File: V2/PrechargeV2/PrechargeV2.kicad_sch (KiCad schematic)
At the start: 51 parts, among them J1 430450428, J2 430450428, J4 436500228, U1 TEA 1-0505E, U2 AMC1351DWVR, U3 AMC1351DWVR, U6 OP284EPZ

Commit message: V2
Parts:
- removed CR1, CR2: B240A-13-F, PreChargeParts:SMA_DIO-L, symbol RelayFlyback:B240A-13-F
- removed MOSFET1, MOSFET2: DMN3404L-7, PreChargeParts:SOT23_DIO-L, symbol RelayFET:DMN3404L-7
- removed U1: TEA 1-0505E, PreChargeParts:TEA 1E_TRP, symbol Isolating DC-DC Converter:TEA_1-0505E
- removed U6: OP284EPZ, OP284:N_8_ADI, symbol OP284:OP284EPZ
- added CR1, CR2: B240A-13-F, RelayDriver:SMA_DIO, symbol RelayDriver:B240A-13-F
- added MOSFET1, MOSFET2: DMN3404L-7, RelayDriver:SOT23_DIO, symbol RelayDriver:DMN3404L-7
- added U1: NMV1S0505SC, 5V-5V:SIP4_NMV1S0_MUR, symbol 5V-5V:NMV1S0505SC
- added U4: TLV9002QDGKRQ1, TLV9002:VSSOP8_DGK_TEX, symbol TLV9002:TLV9002QDGKRQ1
- R1, R10, R11, R12, R13, R14, R15, R16, R17, R18, R2, R21, R22, R23, R24, R25, R26, R27, R28, R3, R4, R5, R6, R7, R8, R9: footprint Resistor_THT:R_Axial_DIN0207_L6.3mm_D2.5mm_P10.16mm_Horizontal -> Resistor_SMD:R_0603_1608Metric_Pad0.98x0.95mm_HandSolder
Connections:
- net +5: now also U1.1 (+VIN), U4.8 (V+)
- net GND: now also MOSFET1.2 (S), MOSFET2.2 (S), U1.2 (-VIN), U4.4 (V-); no longer J1.4
- net HV+5: now also U1.7 (+VOUT)
- net HVGND: now also U1.5 (-VOUT); no longer R6.1, U2.3 (GND1), U2.4 (GND1)
- net ShutdownIn: now also J1.3, CR1.1, CR2.1; no longer J1.1
- net at C10.1, R21.2, R23.2: now also U4.5 (IN2+)
- net at C9.1, R22.2, R24.2: now also U4.6 (IN2-)
- net at C6.1, R10.2, R12.2: now also U4.3 (IN1+)
- net at C7.1, R11.2, R9.2: now also U4.2 (IN1-)
- net at R25.2, R26.1: now also MOSFET1.1 (G)
- net at J1.2: now also CR1.2, MOSFET1.3 (D)
- net at A1.A2, C9.2, R24.1: now also U4.7 (OUT2)
- net at A1.A7, C7.2, R11.1: now also U4.1 (OUT1)
- net at R27.1: now also A1.D9; no longer A1.D3
- net at R27.2, R28.1: now also MOSFET2.1 (G)
- net nCS: now reaches A1.D10
- net SI: now reaches A1.D11 (D11_MOSI)
- net SO: now reaches A1.D12 (D12_MISO)
- net SCK: now reaches A1.D13 (D13_SCK)
- net CANInt: now reaches A1.D8
- net InverterGND renamed INVGND
- net INVGND: now also R6.1, U2.3 (GND1), U2.4 (GND1)
- new net: CR2.2, J1.1, MOSFET2.3 (D)
- new net PrechargeStatus: A1.D3, J1.4
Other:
- added sheet CANBUS (CANBUS.kicad_sch)
- moved on the sheet: C11, C12, R7, R8

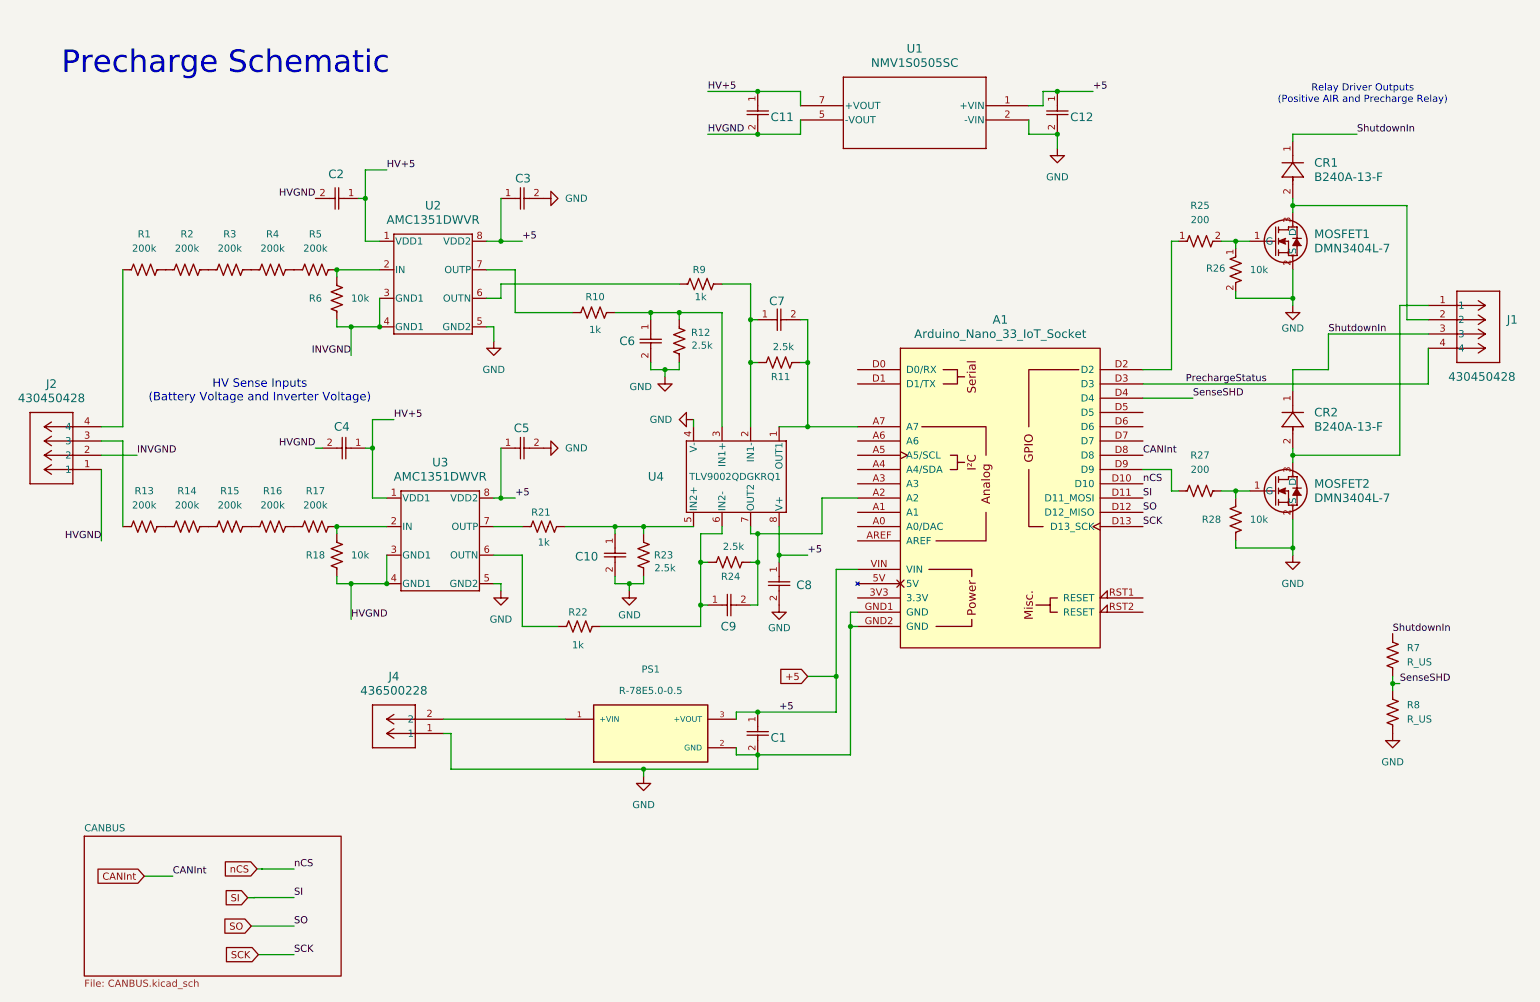
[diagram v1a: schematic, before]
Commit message: Updated Schematic For ESF
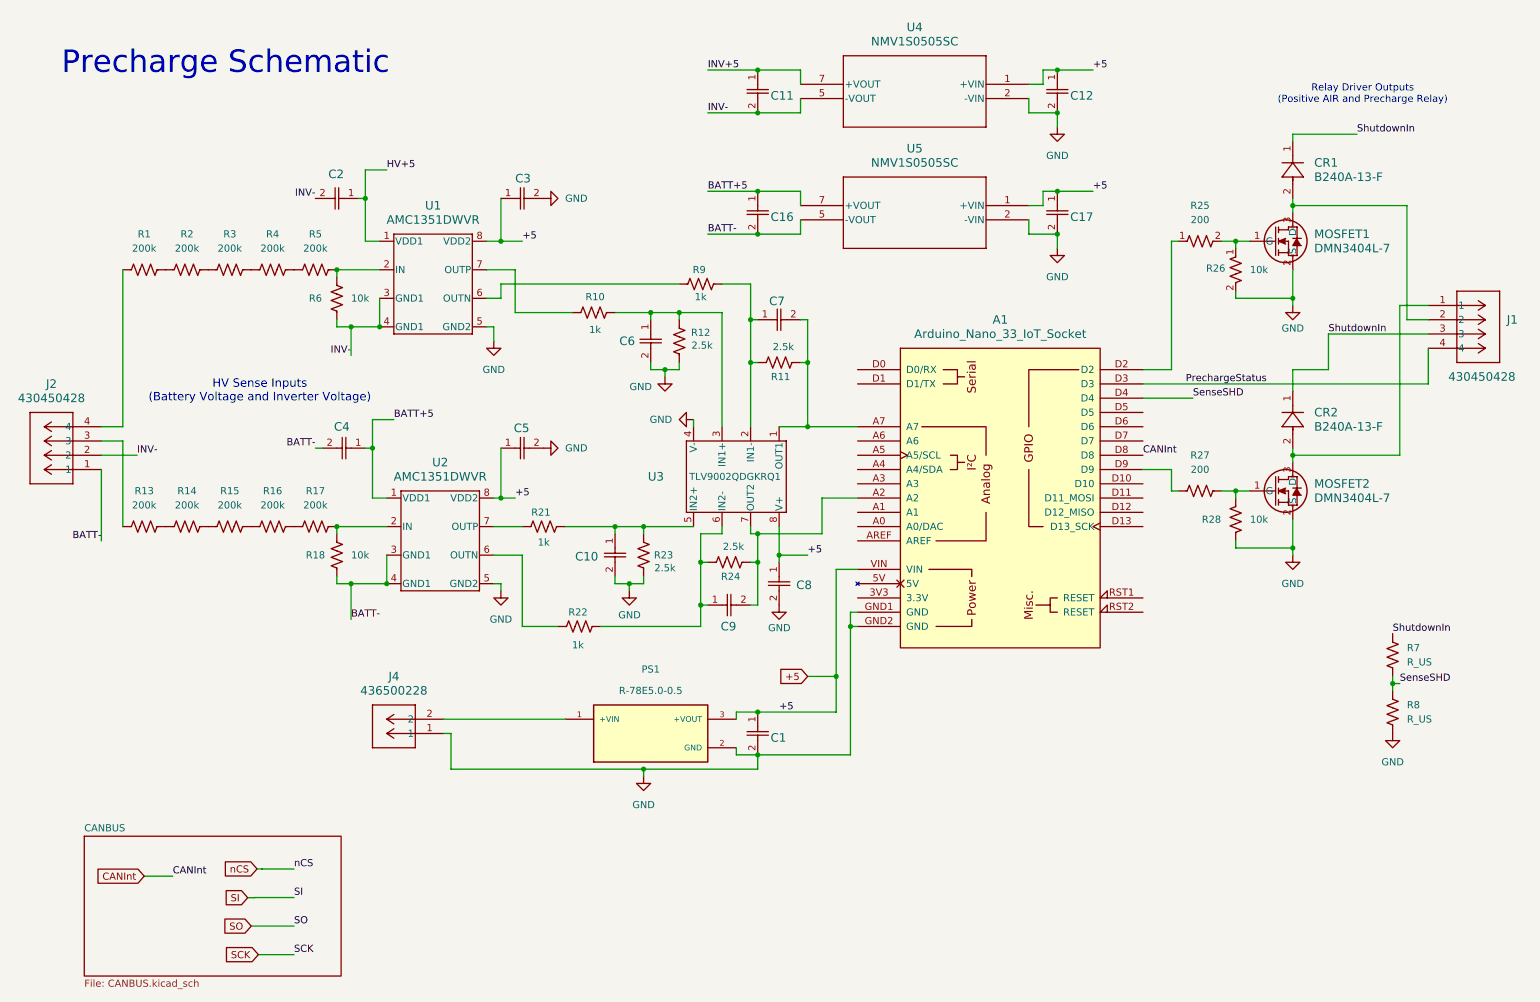
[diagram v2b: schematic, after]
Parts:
- added C16, C17: C324C106K3R5TA, 10uF Cap:CAP_C324C_MR_X7R_KEM, symbol 10uF Cap:C324C106K3R5TA
- added U5: NMV1S0505SC, 5V-5V:SIP4_NMV1S0_MUR, symbol 5V-5V:NMV1S0505SC
- renumbered U2 to U1, U3 to U2, U4 to U3, U1 to U4
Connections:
- net +5: now also C17.1, U5.1 (+VIN)
- net GND: now also C17.2, U5.2 (-VIN)
- net HV+5: no longer C11.1, C4.1, U2.1 (VDD1), U4.7 (+VOUT)
- net SCK: no longer A1.D13 (D13_SCK)
- net SI: no longer A1.D11 (D11_MOSI)
- net SO: no longer A1.D12 (D12_MISO)
- net nCS: no longer A1.D10
- net HVGND renamed BATT-
- net BATT-: now also C16.2, U5.5 (-VOUT); no longer C11.2, C2.2, U4.5 (-VOUT)
- net INVGND renamed INV-
- net INV-: now also C11.2, C2.2, U4.5 (-VOUT)
- new net BATT+5: C16.1, C4.1, U2.1 (VDD1), U5.7 (+VOUT)
- new net INV+5: C11.1, U4.7 (+VOUT)
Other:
- moved on the sheet: C11, C12, U4
